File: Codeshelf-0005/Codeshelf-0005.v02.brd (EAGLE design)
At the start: 140.1 x 99 mm, 53 parts, among them J1 M05X2PTH, J2 RJ45-8PTH, J3-WAKE M02PTH, J4 RJ45-8PTH, J5 HEADER-2X-2.54MM, U1 ZSFM201-1A, U2 MAX232SOIC16, U3 RS485SOIC, U4 ULN2003AD, U5 MIC94061C6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

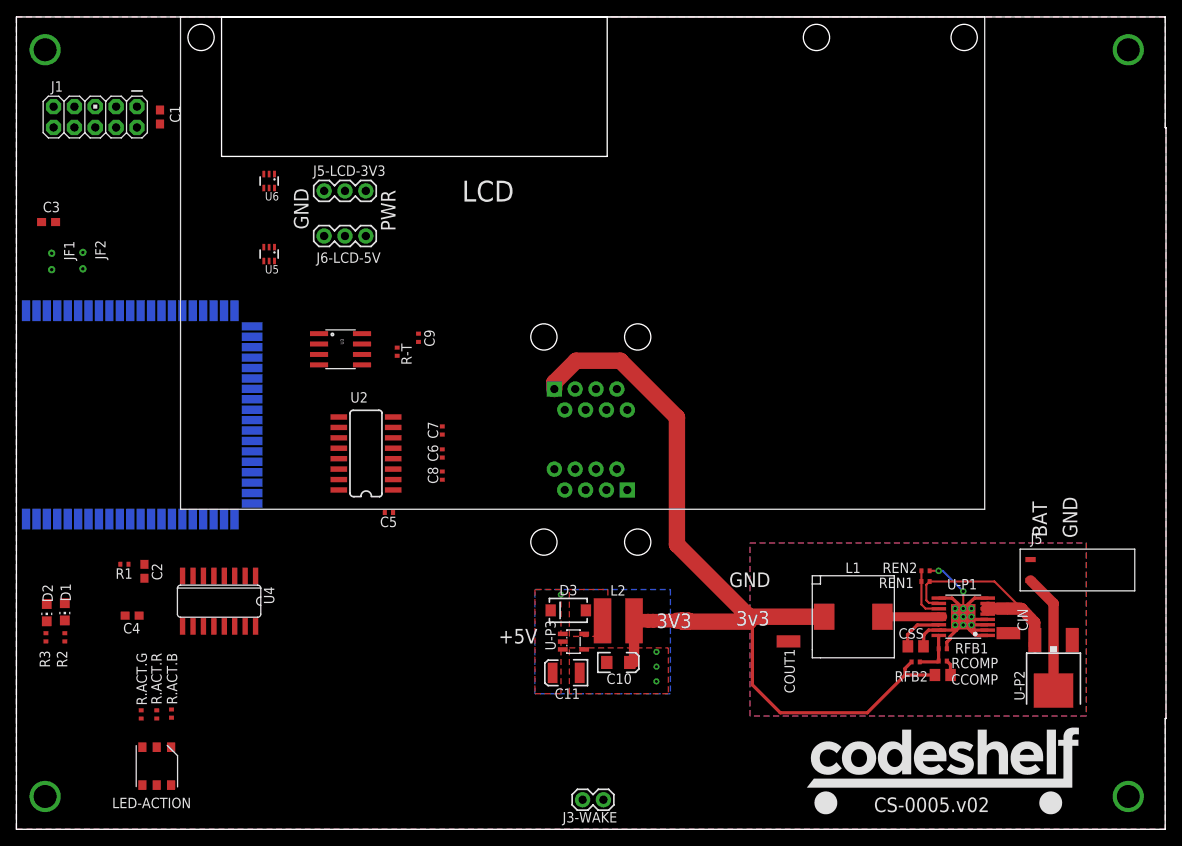
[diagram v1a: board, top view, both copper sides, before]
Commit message: CHE controller changes for Ravi & Charlie feedback
RS485 3V/GND on two conductors
Scanner pins separated from RS485 pins on EN patch cables.
Sleep switch and power control of scanner the LCD display
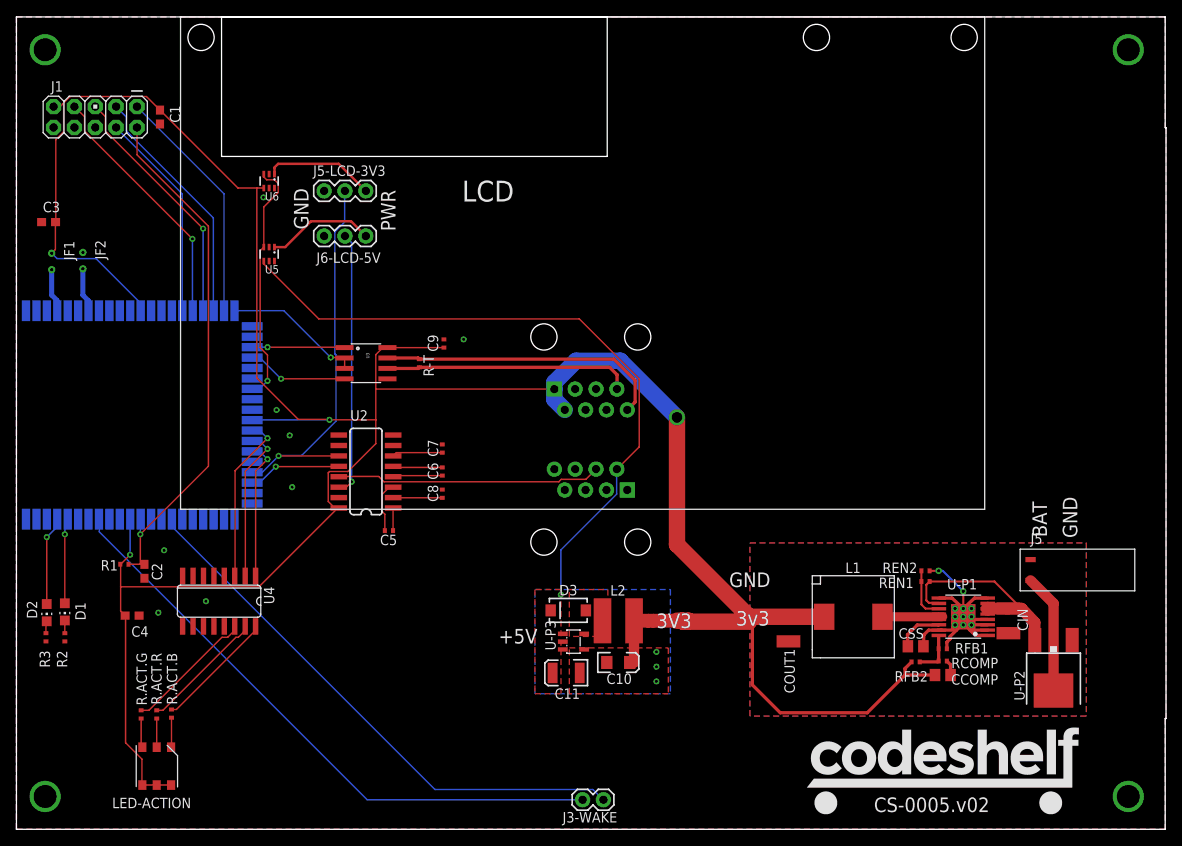
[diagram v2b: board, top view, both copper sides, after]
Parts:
- moved U3 3.54 mm to (52.6, 61.8)
- moved C9 3.18 mm to (62.1, 64.2), turned to 90 degrees
- moved R-T 3.04 mm to (59.1, 61.8)
- moved C5 2.20 mm to (55.4, 41.4)
- moved C7 2.20 mm to (61.9, 51.4)
- moved C8 2.20 mm to (61.9, 45.9)
- moved C6 2.20 mm to (61.9, 48.6)
- moved U2 2.20 mm to (52.6, 48.6)
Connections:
- net +3V3: now also J4.2
- net GND: now also J4.3, J4.6; no longer J4.8
- net N$20: now also J4.8; no longer J4.4
- net N$21: now also J4.7; no longer J4.5
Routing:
- net +3V3: track 128.9 -> 366.9 mm, vias 0 -> 3
- net +5V: track 0.04 -> 82.2 mm
- net N$16: track 0.00 -> 74.0 mm
- net N$14: track 0.00 -> 67.3 mm
- net RESET: track 0.00 -> 64.1 mm, vias 0 -> 1
- net T1IN: track 0.00 -> 48.8 mm, vias 0 -> 1
- net N$20: track 0.00 -> 35.3 mm
- net R1IN: track 0.00 -> 32.3 mm
- net T1OUT: track 0.00 -> 32.1 mm, vias 0 -> 1
- net TDO: track 0.00 -> 30.9 mm, vias 0 -> 1
- net TDI: track 0.00 -> 30.3 mm, vias 0 -> 1
- net N$21: track 0.00 -> 30.2 mm
- net N$9: track 0.00 -> 30.0 mm, vias 0 -> 1
- net TCK: track 0.00 -> 29.8 mm
- net TMS: track 0.00 -> 29.3 mm
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
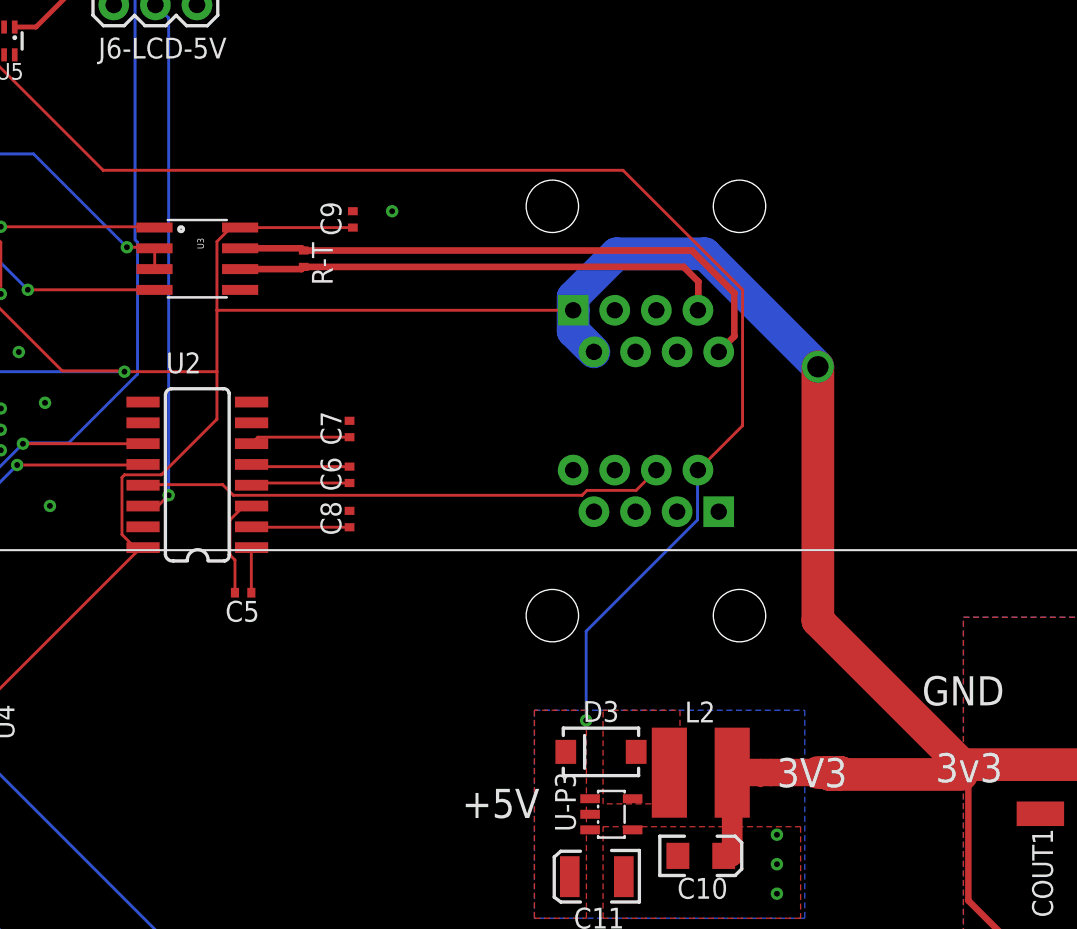
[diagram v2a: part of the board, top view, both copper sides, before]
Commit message: Move the scanner and rs485 connectors to fit around either battery holder type
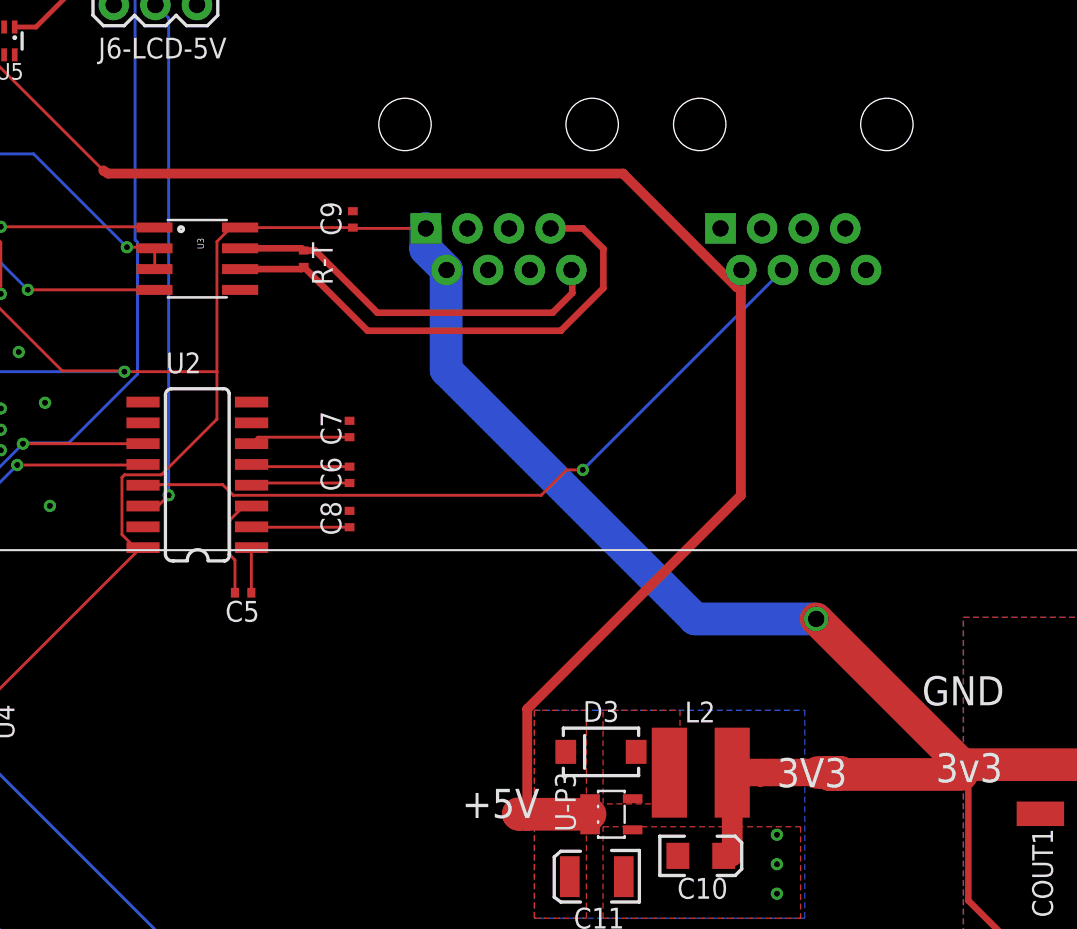
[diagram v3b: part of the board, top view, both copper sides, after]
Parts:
- moved J2 31.3 mm to (89.0, 70.0), turned to 180 degrees
- moved J4 10.3 mm to (71.0, 70.0)
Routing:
- net +3V3: track 366.9 -> 349.7 mm
- net R1IN: track 32.3 -> 45.1 mm, vias 0 -> 1
- net +5V: track 82.2 -> 94.8 mm, vias 1 -> 0
- net N$20: track 35.3 -> 23.8 mm
- net N$21: track 30.2 -> 31.1 mm
- net GND: vias 22 -> 21

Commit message: Changes reviewed with Charlie
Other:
- board text added: "CS0005.2013.11.24.n1"
- board text removed: "CS-0005.v02"
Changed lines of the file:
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@@
 <wire x1="150" y1="5" x2="150" y2="18.5" width="0" layer="20"/>
 <wire x1="150" y1="18.5" x2="150.1" y2="18.5" width="0" layer="20"/>
-<text x="114.5" y="7.1" size="1.778" layer="21">CS-0005.v02</text>
+<text x="148.2" y="49.5" size="1.778" layer="21" rot="R90">CS0005.2013.11.24.n1</text>
 <text x="45.6" y="78.1" size="1.778" layer="21" font="vector" rot="R90">GND</text>
 <text x="56.2" y="77.9" size="1.778" layer="21" font="vector" rot="R90">PWR</text>

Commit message: BOM review before first articles of 0005, 0007, 0008, 0012
Reviewed BOM with Charlie
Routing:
- net +5V: track 94.8 -> 93.0 mm
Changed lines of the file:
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@@
 <element name="C1" library="GW-devices" package="C0603" value="100pF" x="27.5" y="91.8" smashed="yes" rot="R270">
 <attribute name="NAME" x="28.7" y="93.2" size="1.27" layer="25" rot="R270"/>
-<attribute name="MFGN" value="Murata" x="27.5" y="91.8" size="1.778" layer="27" rot="R270" display="off"/>
+<attribute name="MFGN" value="Kemet" x="27.5" y="91.8" size="1.778" layer="27" rot="R270" display="off"/>
 <attribute name="MFGP" value="C0603C101K5RACTU" x="27.5" y="91.8" size="1.778" layer="27" rot="R270" display="off"/>
 </element>
 <element name="C2" library="GW-devices" package="C0603" value="1nF" x="25.6" y="36.44" smashed="yes" rot="R270">
 <attribute name="NAME" x="26.5" y="37.44" size="1.27" layer="25" rot="R270"/>
-<attribute name="MFGN" value="Murata" x="25.6" y="36.44" size="1.778" layer="27" rot="R270" display="off"/>
+<attribute name="MFGN" value="Kemet" x="25.6" y="36.44" size="1.778" layer="27" rot="R270" display="off"/>
 <attribute name="MFGP" value="C0603C102K4RACTU" x="25.6" y="36.44" size="1.778" layer="27" rot="R270" display="off"/>
 </element>
@@
 <element name="C3" library="GW-devices" package="C0603" value="100pF" x="13.92" y="79" smashed="yes">
 <attribute name="NAME" x="13.22" y="80.2" size="1.27" layer="25"/>
-<attribute name="MFGN" value="Murata" x="13.92" y="79" size="1.778" layer="27" display="off"/>
+<attribute name="MFGN" value="Kemet" x="13.92" y="79" size="1.778" layer="27" display="off"/>
 <attribute name="MFGP" value="C0603C101K5RACTU" x="13.92" y="79" size="1.778" layer="27" display="off"/>
 </element>
 <element name="C4" library="GW-devices" package="C0603" value="100pF" x="24.1" y="31.04" smashed="yes" rot="R180">
 <attribute name="NAME" x="26.1" y="29.74" size="1.27" layer="25" rot="R180"/>
-<attribute name="MFGN" value="Murata" x="24.1" y="31.04" size="1.778" layer="27" rot="R180" display="off"/>
+<attribute name="MFGN" value="Kemet" x="24.1" y="31.04" size="1.778" layer="27" rot="R180" display="off"/>
 <attribute name="MFGP" value="C0603C101K5RACTU" x="24.1" y="31.04" size="1.778" layer="27" rot="R180" display="off"/>
 </element>
-<element name="LOGO" library="GW-devices" package="CODESHELF-LOGO" value="CODESHELF-LOGO" x="106.34" y="6.84"/>
+<element name="LOGO" library="GW-devices" package="CODESHELF-LOGO" value="CODESHELF-LOGO" x="106.34" y="6.84">
+<attribute name="NOTES" value="DNP" x="106.34" y="6.84" size="1.778" layer="27" display="off"/>
+</element>
 <element name="C5" library="GW-devices" package="C0402" value=".1uF" x="55.4" y="41.4" smashed="yes" rot="R180">
 <attribute name="NAME" x="56.4" y="40.9" size="1.27" layer="25" rot="R180"/>
@@
 <attribute name="NAME" x="21.66" y="7.575" size="1.27" layer="25"/>
 <attribute name="PRICE" value="0.25" x="44.1" y="19.8" size="1.778" layer="27" rot="R270" display="off"/>
+<attribute name="MFGN" value="BiVar" x="27.1" y="12.7" size="1.778" layer="27" rot="R270" display="off"/>
+<attribute name="MFGP" value="SMP6-RGB" x="27.1" y="12.7" size="1.778" layer="27" rot="R270" display="off"/>
 </element>
 <element name="U4" library="uln-udn" package="SO16" value="ULN2003AD" x="34.7" y="32.8" smashed="yes" rot="R180">
@@
 <wire x1="40.15" y1="73.9" x2="40.15" y2="74.25" width="0.1778" layer="1"/>
 <wire x1="46.85" y1="67.2" x2="40.15" y2="73.9" width="0.1778" layer="1"/>
-<wire x1="76.5889" y1="27.87" x2="72.75" y2="27.87" width="2" layer="1"/>
 <wire x1="72.75" y1="27.87" x2="72.23" y2="27.87" width="2" layer="1"/>
-<wire x1="72.23" y1="27.87" x2="72.2" y2="27.9" width="2" layer="1"/>
+<wire x1="72.23" y1="27.87" x2="74.3" y2="27.9" width="2" layer="1"/>
 <wire x1="46.9" y1="67.15" x2="46.85" y2="67.2" width="0.6" layer="1"/>
 <wire x1="85.8" y1="47.35" x2="85.8" y2="60.05" width="0.6" layer="1"/>
